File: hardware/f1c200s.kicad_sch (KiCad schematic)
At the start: 46 parts, among them J1 Micro_SD_Card, J10 Conn_01x07, J11 Conn_02x05_Odd_Even, J12 Conn_02x03_Odd_Even, J2 USB_B_Micro, J3 Conn_01x03, J4 Conn_01x07, J5 Jumper, J6 Jumper, J7 Jumper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

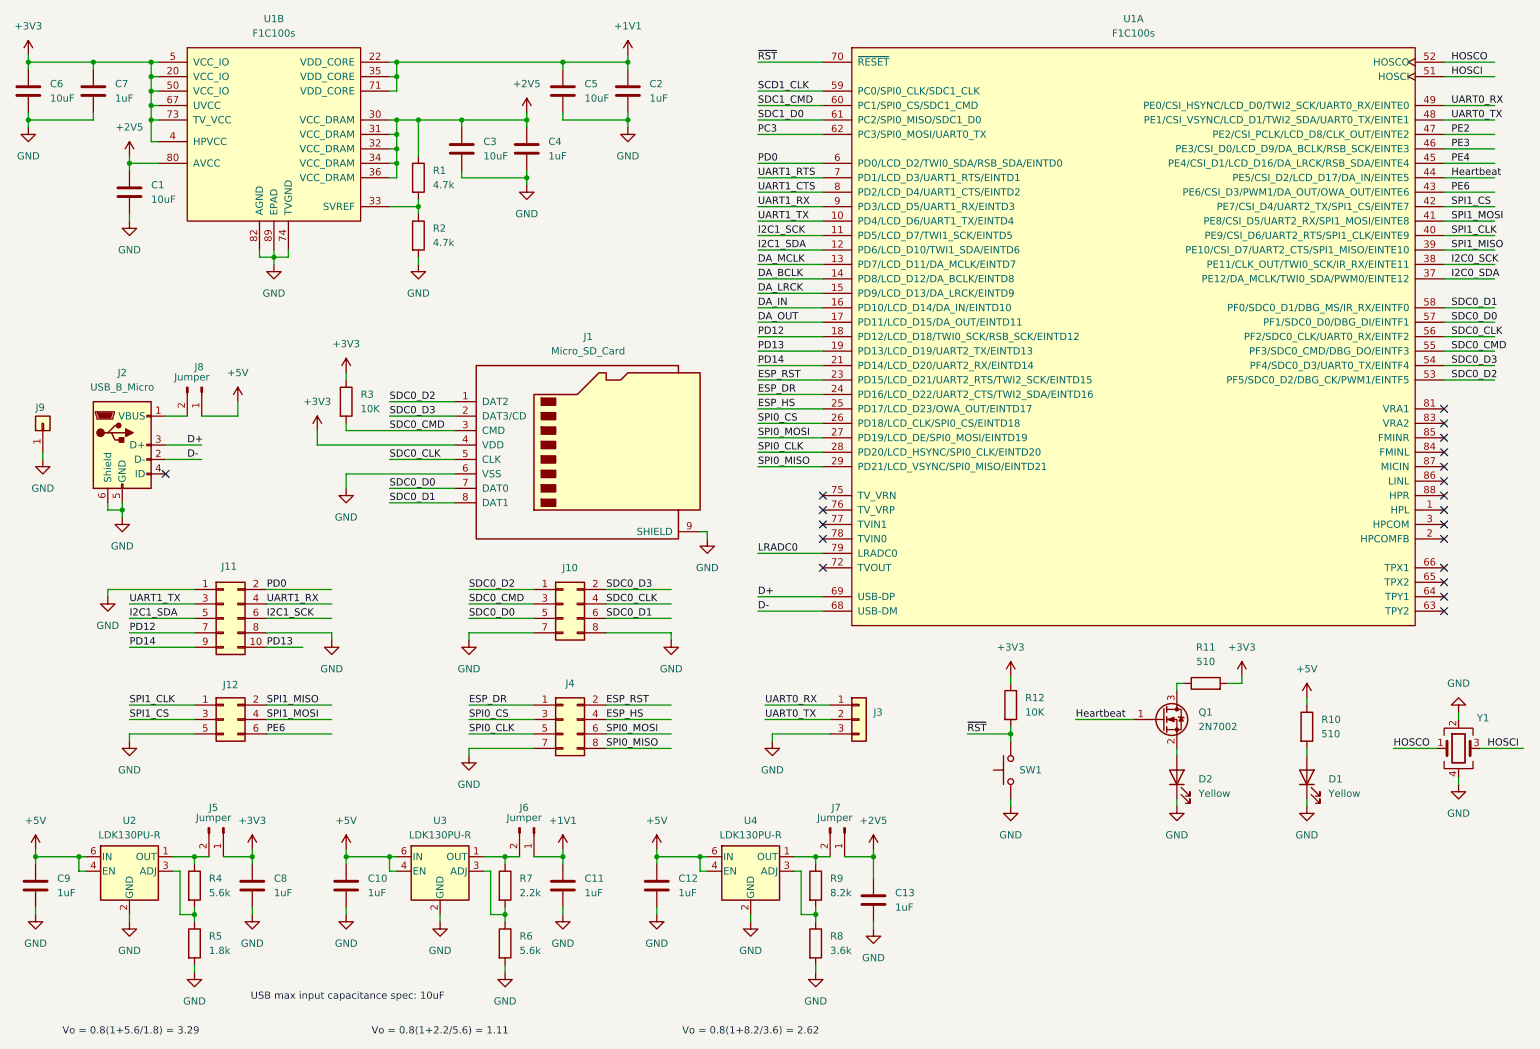
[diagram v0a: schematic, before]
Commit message: Adding ESP32 to board, work in progress
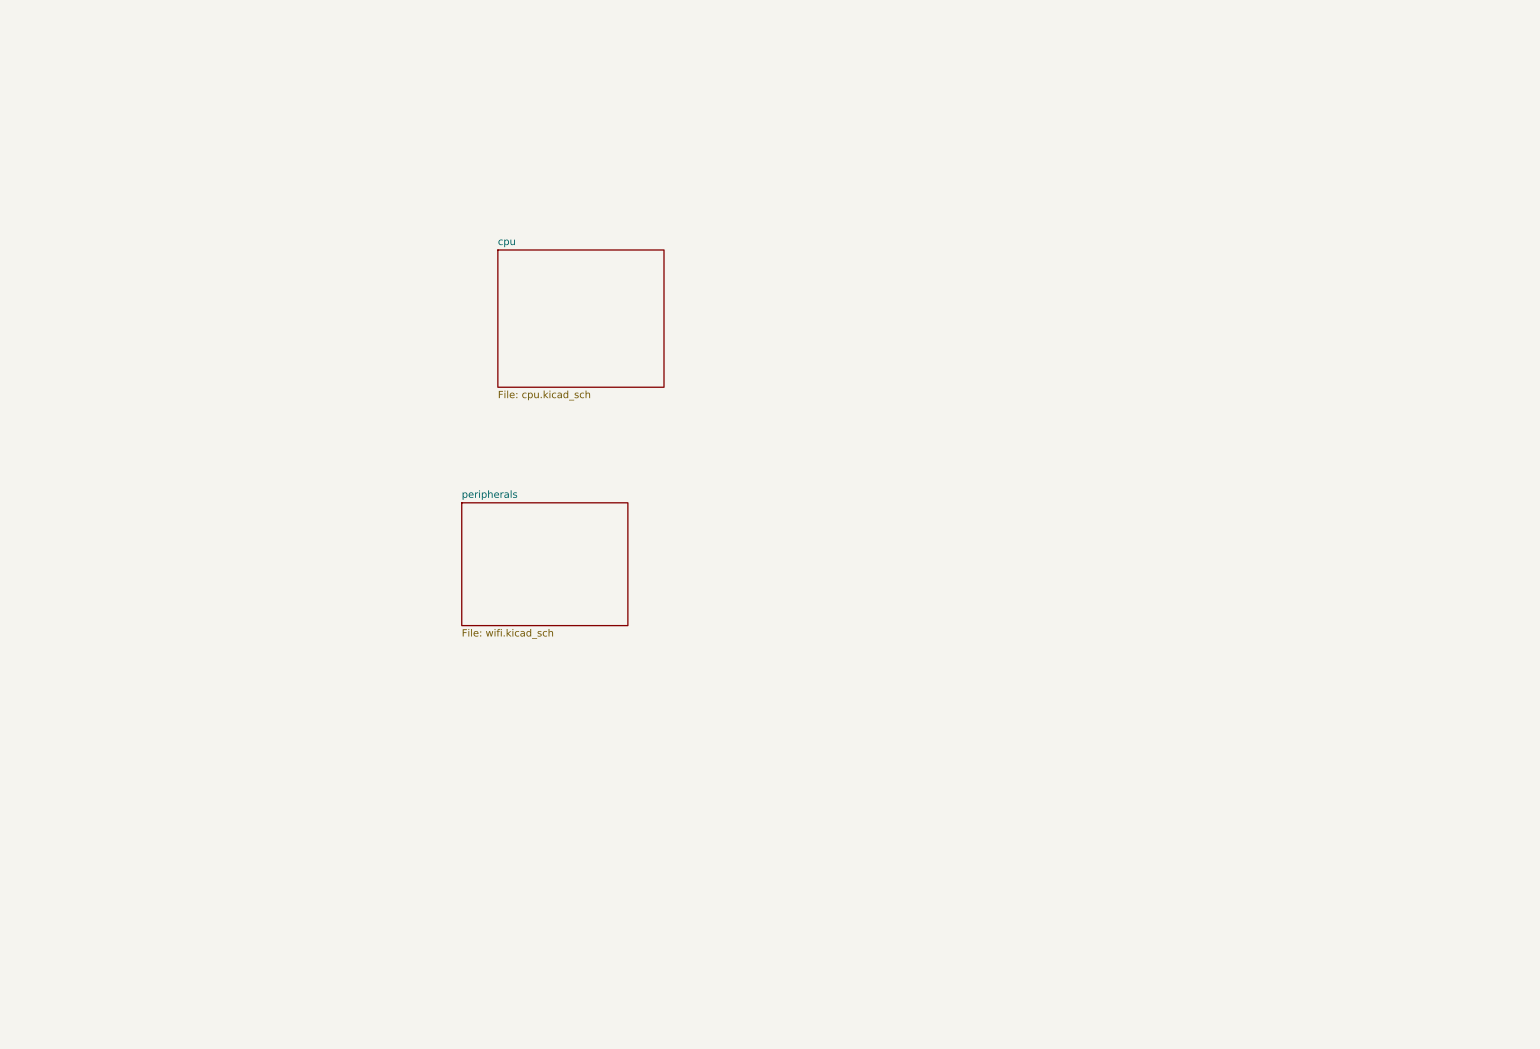
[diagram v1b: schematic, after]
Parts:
- removed C1, C3, C5, C6: 10uF, Capacitor_SMD:C_0402_1005Metric, symbol Device:C
- removed C10, C11, C12, C13, C2, C4, C7, C8, C9: 1uF, Capacitor_SMD:C_0402_1005Metric, symbol Device:C
- removed D1, D2: Yellow, LED_SMD:LED_0603_1608Metric, symbol Device:LED
- removed J1: Micro_SD_Card, Connector_Card:microSD_HC_Molex_104031-0811, symbol Connector:Micro_SD_Card
- removed J10, J4: Conn_01x07, Connector_PinHeader_2.54mm:PinHeader_2x04_P2.54mm_Vertical, symbol Connector_Generic:Conn_02x04_Odd_Even
- removed J11: Conn_02x05_Odd_Even, Connector_PinHeader_2.54mm:PinHeader_2x05_P2.54mm_Vertical, symbol Connector_Generic:Conn_02x05_Odd_Even
- removed J12: Conn_02x03_Odd_Even, Connector_PinHeader_2.54mm:PinHeader_2x03_P2.54mm_Vertical, symbol Connector_Generic:Conn_02x03_Odd_Even
- removed J2: USB_B_Micro, Connector_USB:USB_Micro-B_Amphenol_10118193-0001LF_Horizontal, symbol Connector:USB_B_Micro
- removed J3: Conn_01x03, Connector_PinHeader_2.54mm:PinHeader_1x03_P2.54mm_Vertical, symbol Connector_Generic:Conn_01x03
- removed J5, J6, J7, J8: Jumper, Connector_PinHeader_2.54mm:PinHeader_1x02_P2.54mm_Vertical, symbol Connector:Conn_01x02_Pin
- removed J9: Conn_01x01, Connector_PinHeader_2.54mm:PinHeader_1x01_P2.54mm_Vertical, symbol Connector_Generic:Conn_01x01
- removed Q1: 2N7002, Package_TO_SOT_SMD:SOT-23, symbol Transistor_FET:2N7002
- removed R1, R2: 4.7k, Resistor_SMD:R_0402_1005Metric, symbol Device:R
- removed R10, R11: 510, Resistor_SMD:R_0603_1608Metric, symbol Device:R
- removed R12, R3: 10K, Resistor_SMD:R_0603_1608Metric, symbol Device:R
- removed R4, R6: 5.6k, Resistor_SMD:R_0603_1608Metric, symbol Device:R
- removed R5: 1.8k, Resistor_SMD:R_0603_1608Metric, symbol Device:R
- removed R7: 2.2k, Resistor_SMD:R_0603_1608Metric, symbol Device:R
- removed R8: 3.6k, Resistor_SMD:R_0603_1608Metric, symbol Device:R
- removed R9: 8.2k, Resistor_SMD:R_0603_1608Metric, symbol Device:R
- removed SW1: SW_Push, Button_Switch_SMD:SW_Push_1P1T_XKB_TS-1187A, symbol Switch:SW_Push
- removed U1: F1C100s, f1c200s:QFN-88_EP_10x10_Pitch0.4mm, symbol f1c200s:F1C100s
- removed U2, U3, U4: LDK130PU-R, Package_DFN_QFN:DFN-6_1.3x1.2mm_P0.4mm, symbol Regulator_Linear:LDK130-ADJ_DFN6
- removed Y1: XRCGB24M000F0G00R0, Crystal:Crystal_SMD_2016-4Pin_2.0x1.6mm, symbol Device:Crystal_GND24
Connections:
- no-connect marks 20 -> 0
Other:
- added sheet cpu (cpu.kicad_sch)
- added sheet peripherals (wifi.kicad_sch)
- note removed: "USB max input capacitance spec: 10uF"
- note removed: "Vo = 0.8(1+2.2/5.6) = 1.11"
- note removed: "Vo = 0.8(1+5.6/1.8) = 3.29"
- note removed: "Vo = 0.8(1+8.2/3.6) = 2.62"
